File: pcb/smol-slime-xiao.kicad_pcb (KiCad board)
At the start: 4 copper layers, 20 x 23.5 mm, 12 parts, among them J1 Conn_01x02, J2 Conn_01x02, U1 ICM-45686, U3 1532H, U4 XIAO-nRF52840-SMD

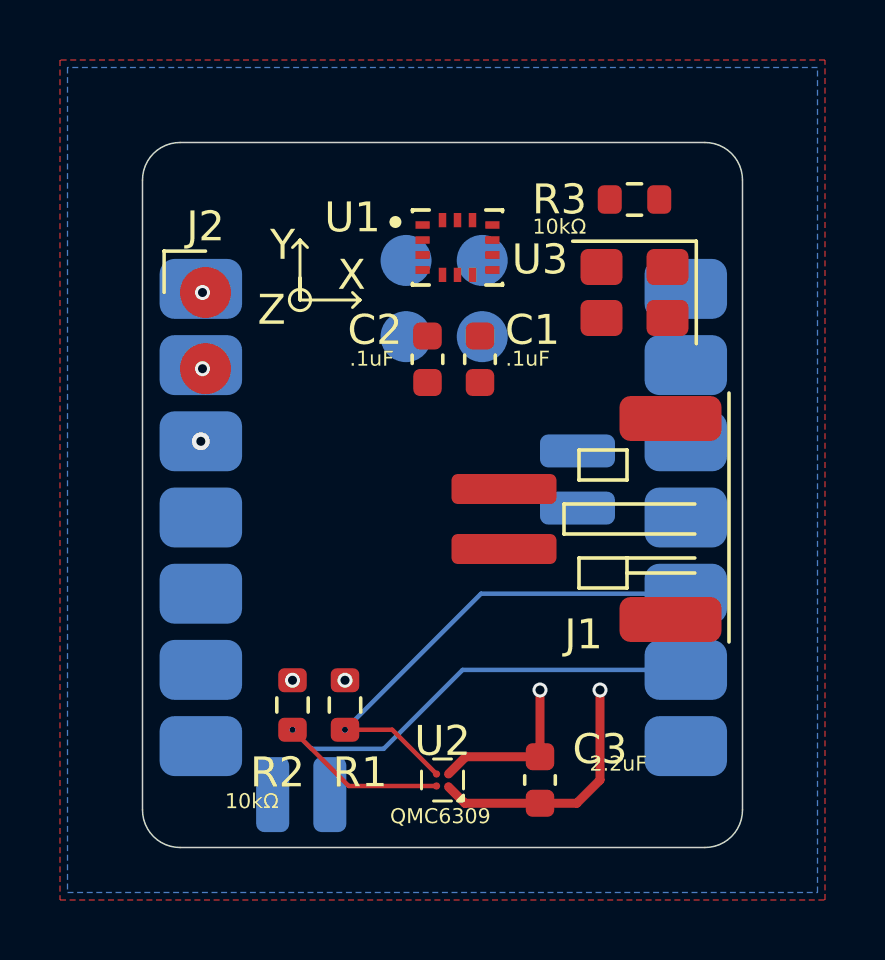
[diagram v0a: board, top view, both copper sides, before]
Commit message: Add JST vias
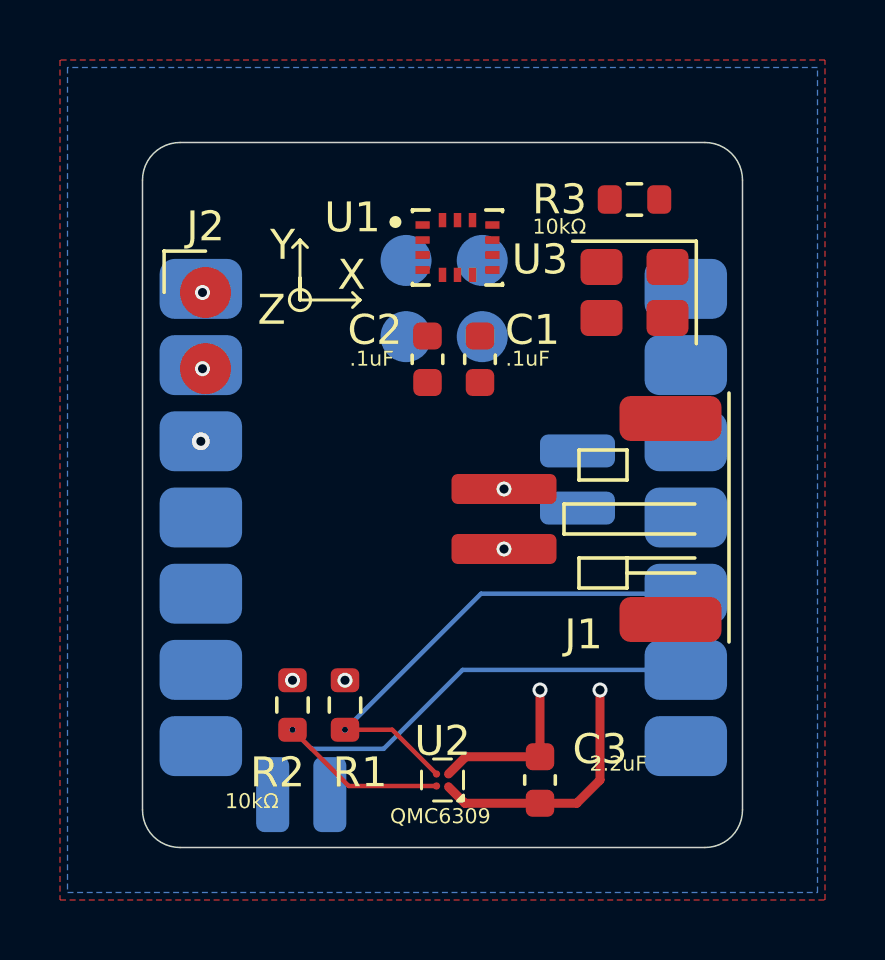
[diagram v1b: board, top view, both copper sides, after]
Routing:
- net GND: vias 2 -> 3
- net /VBAT: vias 0 -> 1
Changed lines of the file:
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@@
+		(net 1)
+	)
+	(via
+		(at 152.05 99.05)
+		(size 0.5)
+		(drill 0.3)
+		(layers "F.Cu" "B.Cu")
 		(net 1)
 	)
@@
 		(net 18)
 	)
+	(via
+		(at 152.05 101.05)
+		(size 0.5)
+		(drill 0.3)
+		(layers "F.Cu" "B.Cu")
+		(net 19)
+	)
 	(zone

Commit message: PCB Current
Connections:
- C2 pad 1: unconnected-(C2-Pad1) -> GND
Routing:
- net GND: vias 3 -> 2
- net +5V: vias 1 -> 0
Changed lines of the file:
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@@
 	(net 18 "+5V")
 	(net 19 "/VBAT")
-	(net 20 "unconnected-(C2-Pad1)")
-	(net 21 "unconnected-(U4-P1.12_D7_RX-Pad8)")
-	(net 22 "unconnected-(U4-NFC1-Pad17)")
-	(net 23 "unconnected-(U4-NFC2-Pad18)")
-	(net 24 "unconnected-(U4-PA31_SWDIO-Pad19)")
-	(net 25 "unconnected-(U4-PA30_SWCLK-Pad20)")
-	(net 26 "unconnected-(U4-P1.11_D6_TX-Pad7)")
-	(net 27 "unconnected-(U4-P0.02_A0_D0-Pad1)")
-	(net 28 "unconnected-(J1-Pin_3-Pad3)")
-	(net 29 "unconnected-(J1-Pin_3-Pad3)_1")
+	(net 20 "unconnected-(U4-P1.12_D7_RX-Pad8)")
+	(net 21 "unconnected-(U4-NFC1-Pad17)")
+	(net 22 "unconnected-(U4-NFC2-Pad18)")
+	(net 23 "unconnected-(U4-PA31_SWDIO-Pad19)")
+	(net 24 "unconnected-(U4-PA30_SWCLK-Pad20)")
+	(net 25 "unconnected-(U4-P1.11_D6_TX-Pad7)")
+	(net 26 "unconnected-(U4-P0.02_A0_D0-Pad1)")
+	(net 27 "unconnected-(J1-Pin_3-Pad3)")
+	(net 28 "unconnected-(J1-Pin_3-Pad3)_1")
 	(footprint "Resistor_SMD:R_0603_1608Metric"
 		(layer "F.Cu")
@@
 			(layers "F.Cu" "F.Mask" "F.Paste")
 			(roundrect_rratio 0.25)
-			(net 28 "unconnected-(J1-Pin_3-Pad3)")
+			(net 28 "unconnected-(J1-Pin_3-Pad3)_1")
 			(pinfunction "Pin_3")
 			(pintype "passive+no_connect")
@@
 			(layers "F.Cu" "F.Mask" "F.Paste")
 			(roundrect_rratio 0.25)
-			(net 29 "unconnected-(J1-Pin_3-Pad3)_1")
+			(net 27 "unconnected-(J1-Pin_3-Pad3)")
 			(pinfunction "Pin_3")
 			(pintype "passive+no_connect")
@@
 			(layers "F.Cu" "F.Mask" "F.Paste")
 			(roundrect_rratio 0.25)
-			(net 20 "unconnected-(C2-Pad1)")
+			(net 1 "GND")
 			(pintype "passive")
 		)
@@
 			(layers "B.Cu" "B.Mask" "B.Paste")
 			(roundrect_rratio 0.25)
-			(net 27 "unconnected-(U4-P0.02_A0_D0-Pad1)")
+			(net 26 "unconnected-(U4-P0.02_A0_D0-Pad1)")
 			(pinfunction "P0.02_A0_D0")
 			(pintype "passive+no_connect")
@@
 			(layers "B.Cu" "B.Mask" "B.Paste")
 			(roundrect_rratio 0.25)
-			(net 26 "unconnected-(U4-P1.11_D6_TX-Pad7)")
+			(net 25 "unconnected-(U4-P1.11_D6_TX-Pad7)")
 			(pinfunction "P1.11_D6_TX")
 			(pintype "passive+no_connect")
@@
 			(layers "B.Cu" "B.Mask" "B.Paste")
 			(roundrect_rratio 0.25)
-			(net 21 "unconnected-(U4-P1.12_D7_RX-Pad8)")
+			(net 20 "unconnected-(U4-P1.12_D7_RX-Pad8)")
 			(pinfunction "P1.12_D7_RX")
 			(pintype "passive+no_connect")
@@
 			(layers "B.Cu" "B.Mask" "B.Paste")
 			(roundrect_rratio 0.25)
-			(net 22 "unconnected-(U4-NFC1-Pad17)")
+			(net 21 "unconnected-(U4-NFC1-Pad17)")
 			(pinfunction "NFC1")
 			(pintype "passive+no_connect")
@@
 			(layers "B.Cu" "B.Mask" "B.Paste")
 			(roundrect_rratio 0.25)
-			(net 23 "unconnected-(U4-NFC2-Pad18)")
+			(net 22 "unconnected-(U4-NFC2-Pad18)")
 			(pinfunction "NFC2")
 			(pintype "passive+no_connect")
@@
 			(size 1.7 1.7)
 			(layers "B.Cu" "B.Mask" "B.Paste")
-			(net 24 "unconnected-(U4-PA31_SWDIO-Pad19)")
+			(net 23 "unconnected-(U4-PA31_SWDIO-Pad19)")
 			(pinfunction "PA31_SWDIO")
 			(pintype "passive+no_connect")
@@
 			(size 1.7 1.7)
 			(layers "B.Cu" "B.Mask" "B.Paste")
-			(net 25 "unconnected-(U4-PA30_SWCLK-Pad20)")
+			(net 24 "unconnected-(U4-PA30_SWCLK-Pad20)")
 			(pinfunction "PA30_SWCLK")
 			(pintype "passive+no_connect")
@@
 	)
 	(via
-		(at 142 95.04)
-		(size 0.5)
-		(drill 0.3)
-		(layers "F.Cu" "B.Cu")
-		(net 1)
-	)
-	(via
 		(at 152.05 99.05)
 		(size 0.5)
@@
 	)
 	(via
-		(at 142 92.5)
-		(size 0.5)
-		(drill 0.3)
-		(layers "F.Cu" "B.Cu")
-		(net 18)
-	)
-	(via

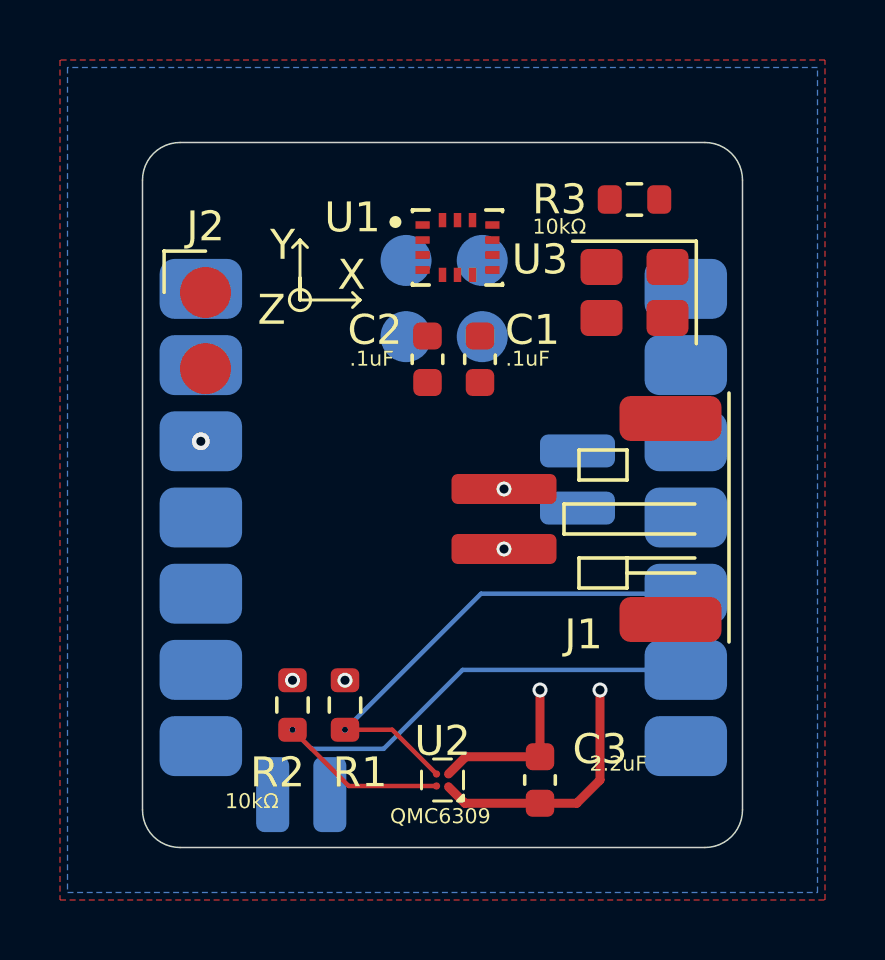
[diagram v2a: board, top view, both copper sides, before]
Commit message: Changed charge connector footprint to 3 pin variant
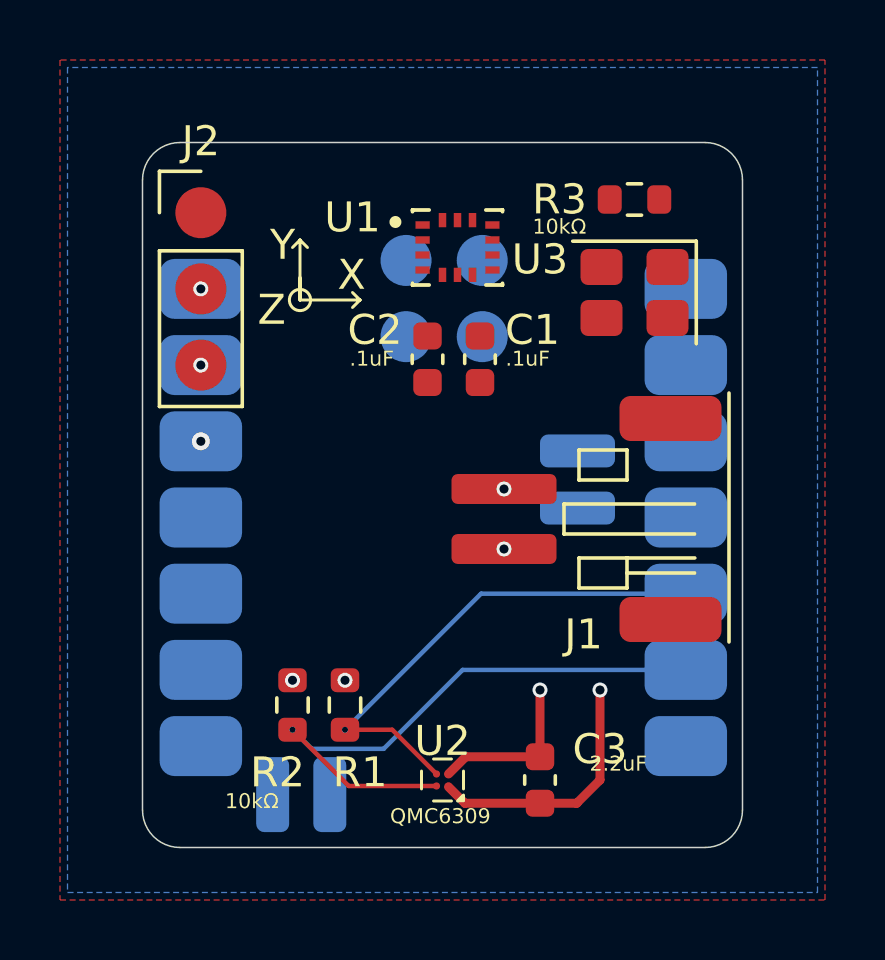
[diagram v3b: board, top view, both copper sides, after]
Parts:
- J1: value Conn_01x02 -> Battery_Terminal
- J2: value Conn_01x02 -> Charger_Connecter; footprint Generic:PinPads_1x02_P2.54mm -> Generic:PinPads_1x03_P2.54mm
- moved J2 2.66 mm to (141.9, 89.8)
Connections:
- J1 pad 2: GND -> /VBAT_GND
- J2 pad 1: +5V -> /VBAT_GND
- J2 pad 2: GND -> +5V
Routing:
- net /VBAT_GND: vias 0 -> 1
- net +5V: vias 0 -> 1
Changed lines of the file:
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@@
 	(net 27 "unconnected-(J1-Pin_3-Pad3)")
 	(net 28 "unconnected-(J1-Pin_3-Pad3)_1")
+	(net 29 "/VBAT_GND")
 	(footprint "Resistor_SMD:R_0603_1608Metric"
 		(layer "F.Cu")
@@
 			)
 		)
-		(property "Value" "Conn_01x02"
+		(property "Value" "Battery_Terminal"
 			(at 1 8.6 90)
 			(layer "F.Fab")
@@
 			(layers "F.Cu" "F.Mask" "F.Paste")
 			(roundrect_rratio 0.2083333333)
-			(net 1 "GND")
+			(net 29 "/VBAT_GND")
 			(pinfunction "Pin_2")
 			(pintype "passive")
@@
 		)
 	)
-	(footprint "Generic:PinPads_1x02_P2.54mm"
+	(footprint "Generic:PinPads_1x03_P2.54mm"
 		(layer "F.Cu")
-		(at 142.1 92.5)
-		(descr "Through hole straight pin header, 1x02, 2.54mm pitch, single row")
-		(tags "Through hole pin header THT 1x02 2.54mm single row")
+		(at 141.945 89.84)
+		(descr "Through hole straight pin header, 1x03, 2.54mm pitch, single row")
+		(tags "Through hole pin header THT 1x03 2.54mm single row")
 		(property "Reference" "J2"
-			(at 0 -2.2 0)
+			(at 0 -2.38 0)
 			(layer "F.SilkS")
 			(effects
@@
 			)
 		)
-		(property "Value" "Conn_01x02"
-			(at 0 4.92 0)
+		(property "Value" "Charger_Connecter"
+			(at 0.7 8.4 0)
 			(layer "F.Fab")
-			(hide yes)
 			(effects
 				(font
@@
 			)
 		)
-		(property "Description" "Generic connector, single row, 01x02, script generated (kicad-library-utils/schlib/autogen/connector/)"
+		(property "Description" "Generic connector, single row, 01x03, script generated (kicad-library-utils/schlib/autogen/connector/)"
 			(at 0 0 0)
 			(layer "F.Fab")
@@
 		)
 		(fp_line
-			(start -1.5 -1.5)
-			(end -1.5 4)
+			(start -1.38 1.27)
+			(end -1.38 6.46)
+			(stroke
+				(width 0.12)
+				(type solid)
+			)
+			(layer "F.SilkS")
+		)
+		(fp_line
+			(start -1.38 1.27)
+			(end 1.38 1.27)
+			(stroke
+				(width 0.12)
+				(type solid)
+			)
+			(layer "F.SilkS")
+		)
+		(fp_line
+			(start -1.38 6.46)
+			(end 1.38 6.46)
+			(stroke
+				(width 0.12)
+				(type solid)
+			)
+			(layer "F.SilkS")
+		)
+		(fp_line
+			(start 1.38 1.27)
+			(end 1.38 6.46)
+			(stroke
+				(width 0.12)
+				(type solid)
+			)
+			(layer "F.SilkS")
+		)
+		(fp_line
+			(start -1.77 -1.77)
+			(end -1.77 6.85)
 			(stroke
 				(width 0.05)
@@
 		)
 		(fp_line
-			(start -1.5 4)
-			(end 1.5 4)
+			(start -1.77 6.85)
+			(end 1.77 6.85)
 			(stroke
 				(width 0.05)
@@
 		)
 		(fp_line
-			(start 1.5 -1.5)
-			(end -1.5 -1.5)
+			(start 1.77 -1.77)
+			(end -1.77 -1.77)
 			(stroke
 				(width 0.05)
@@
 		)
 		(fp_line
-			(start 1.5 4)
-			(end 1.5 -1.5)
+			(start 1.77 6.85)
+			(end 1.77 -1.77)
 			(stroke
 				(width 0.05)
@@
 		)
 		(fp_line
-			(start -1.27 3.81)
+			(start -1.27 6.35)
 			(end -1.27 -0.635)
 			(stroke
@@
 		(fp_line
 			(start 1.27 -1.27)
-			(end 1.27 3.81)
+			(end 1.27 6.35)
 			(stroke
 				(width 0.1)
@@
 		)
 		(fp_line
-			(start 1.27 3.81)
-			(end -1.27 3.81)
+			(start 1.27 6.35)
+			(end -1.27 6.35)
 			(stroke
 				(width 0.1)
@@
 		)
 		(fp_text user "${REFERENCE}"
-			(at 0 -2.25 180)
+			(at 3 2.2 90)
 			(layer "F.Fab")
 			(effects
@@
 			(size 1.7 1.7)
 			(layers "F.Cu" "F.Mask" "F.Paste")
-			(net 18 "+5V")
+			(net 29 "/VBAT_GND")
 			(pinfunction "Pin_1")
 			(pintype "passive")
@@
 			(size 1.7 1.7)
 			(layers "F.Cu" "F.Mask" "F.Paste")
-			(net 1 "GND")
+			(net 18 "+5V")
 			(pinfunction "Pin_2")
 			(pintype "passive")
 		)
+		(pad "3" smd circle
+			(at 0 5.08)
+			(size 1.7 1.7)
+			(layers "F.Cu" "F.Mask" "F.Paste")
+			(net 1 "GND")
+			(pinfunction "Pin_3")
+			(pintype "passive")
+		)
 		(embedded_fonts no)
+		(model "${KICAD9_3DMODEL_DIR}/Connector_PinHeader_2.54mm.3dshapes/PinHeader_1x03_P2.54mm_Vertical.step"
+			(offset
+				(xyz 0 0 0)
+			)
+			(scale
+				(xyz 1 1 1)
+			)
+			(rotate
+				(xyz 0 0 0)
+			)
+		)
 	)
 	(footprint "Capacitor_SMD:C_0603_1608Metric"
@@
 	)
 	(via
-		(at 152.05 99.05)
+		(at 141.945 94.92)
 		(size 0.5)
 		(drill 0.3)
@@
 	)
 	(via
+		(at 141.945 92.38)
+		(size 0.5)
+		(drill 0.3)
+		(layers "F.Cu" "B.Cu")
+		(net 18)
+	)
+	(via
 		(at 152.05 101.05)
 		(size 0.5)
@@
 		(net 19)
 	)
+	(via
+		(at 152.05 99.05)
+		(size 0.5)
+		(drill 0.3)
+		(layers "F.Cu" "B.Cu")
+		(net 29)
+	)
 	(zone

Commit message: Add power switch
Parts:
- added SW1: Power_Switch, SW_SSSS811101:SW_SSSS811101, F.Cu at (150.0, 89.8)
- moved R3 10.9 mm to (146.2, 93.5)
- moved U3 10.8 mm to (146.2, 96.2)
- moved U1 10.0 mm to (145.8, 99.8)
- moved C1 9.42 mm to (146.8, 103.0)
- moved C2 9.42 mm to (145.0, 103.0)
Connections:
- J1 pad 2: /VBAT_GND -> Net-(J1-Pin_2)
- J2 pad 1: /VBAT_GND -> Net-(J2-Pin_1)
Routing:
- net Net-(J1-Pin_2): vias 0 -> 1
- net /VBAT_GND: vias 1 -> 0

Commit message: Reorganise PCB
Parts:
- moved R3 10.9 mm to (156.8, 90.5), turned to -90 degrees
- moved C1 8.81 mm to (147.8, 94.2), turned to -90 degrees
- moved C2 8.75 mm to (145.2, 94.2), turned to -90 degrees
- moved R1 8.00 mm to (154.8, 106.2)
- moved R2 8.00 mm to (153.0, 106.2)
- moved U3 7.65 mm to (153.8, 94.8)
- moved C3 6.28 mm to (147.0, 109.0), turned to 0 degrees
- moved U1 1.85 mm to (146.0, 98.0), turned to 180 degrees
- moved SW1 0.25 mm to (150.0, 89.5)
- turned U2 to 180 degrees
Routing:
- net /SPI_CS_IMU: track 0.00 -> 17.5 mm, vias 0 -> 1
- net /IMU_INT: track 0.00 -> 15.5 mm, vias 0 -> 1
- net /IMU_CLKIN: track 0.00 -> 10.8 mm, vias 0 -> 2
- net /SPI_SCK: track 0.00 -> 9.79 mm, vias 0 -> 1
- net /I2C_SCL: track 20.0 -> 10.4 mm
- net /CLK_CTL: track 0.00 -> 9.21 mm, vias 0 -> 1
- net /SPI_MISO: track 0.00 -> 9.19 mm, vias 0 -> 1
- net Net-(J1-Pin_2): track 0.00 -> 8.71 mm
- net Net-(J2-Pin_1): track 0.00 -> 7.51 mm
- net /SPI_MOSI: track 0.00 -> 6.97 mm, vias 0 -> 1
- net VDD: track 5.51 -> 10.5 mm, vias 4 -> 9
- net /I2C_SDA: track 16.9 -> 13.5 mm
- net /VBAT: track 0.00 -> 3.01 mm
- net GND: track 8.60 -> 10.7 mm, vias 2 -> 5

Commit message: Tied ground vias
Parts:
- added J3: Conn_01x01, Generic:Heat_Pad_1.0x1.0mm, F.Cu at (155.0, 99.8)
- added J4: Conn_01x01, Generic:Heat_Pad_1.0x1.0mm, F.Cu at (155.0, 98.0)
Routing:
- net GND: vias 5 -> 44
- net /VBAT: vias 1 -> 2

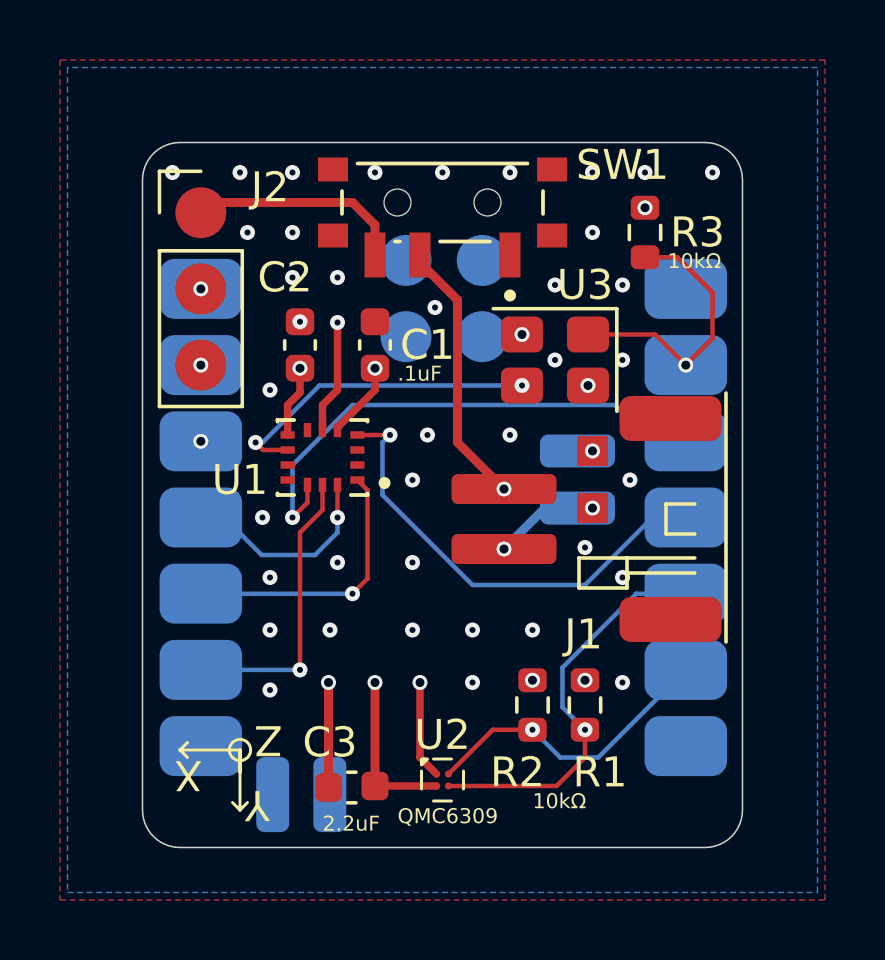
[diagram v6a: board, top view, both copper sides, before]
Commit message: Balance VDD plane GND via cutoffs
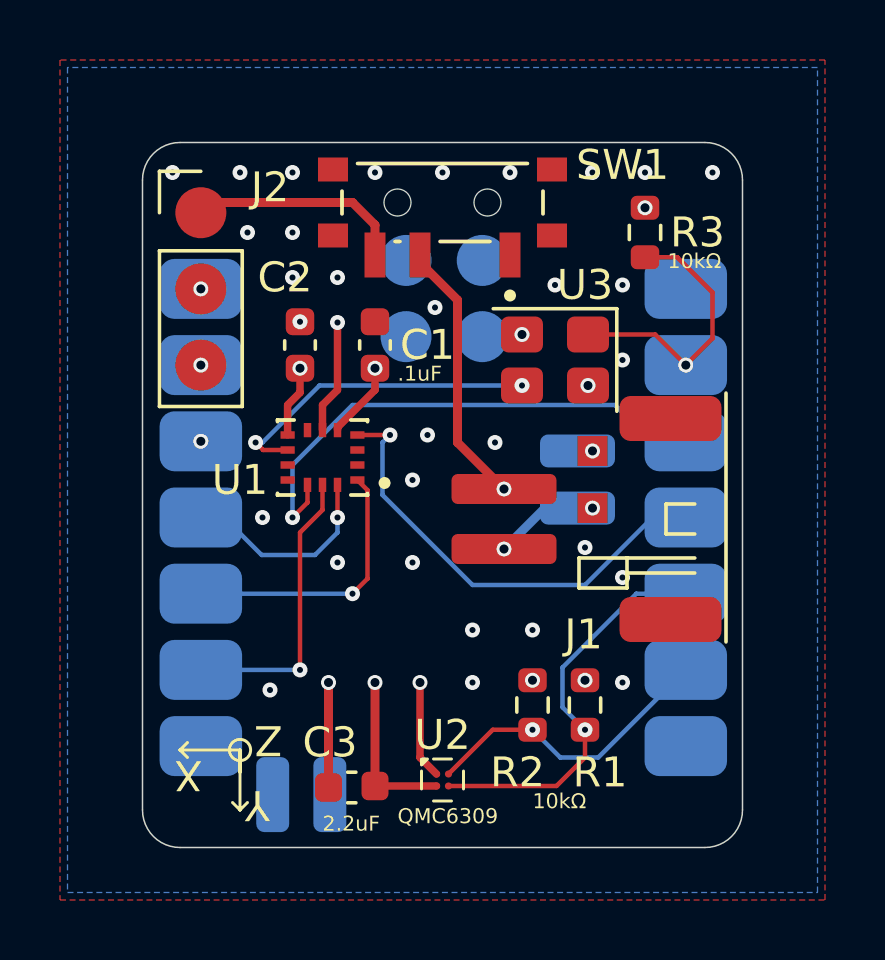
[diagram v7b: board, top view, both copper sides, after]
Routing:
- net GND: vias 44 -> 36
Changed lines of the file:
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@@
-	)
-	(via
-		(at 144.25 103.75)
-		(size 0.5)
-		(drill 0.2)
-		(layers "F.Cu" "B.Cu")
-		(free yes)
-		(net 1)
 	)
 	(via
@@
 	)
 	(via
-		(at 144.25 102)
-		(size 0.5)
-		(drill 0.2)
-		(layers "F.Cu" "B.Cu")
-		(free yes)
-		(net 1)
-	)
-	(via
 		(at 146.5 92)
 		(size 0.5)
@@
 	)
 	(via
-		(at 155 90.5)
-		(size 0.5)
-		(drill 0.2)
-		(layers "F.Cu" "B.Cu")
-		(free yes)
-		(net 1)
-	)
-	(via
 		(at 151 105.5)
 		(size 0.5)
@@
 	)
 	(via
-		(at 149 103.75)
-		(size 0.5)
-		(drill 0.2)
-		(layers "F.Cu" "B.Cu")
-		(free yes)
-		(net 1)
-	)
-	(via
 		(at 151 103.75)
 		(size 0.5)
@@
 	)
 	(via
-		(at 156.25 98.75)
-		(size 0.5)
-		(drill 0.2)
-		(layers "F.Cu" "B.Cu")
-		(free yes)
-		(net 1)
-	)
-	(via
-		(at 144.25 95.75)
-		(size 0.5)
-		(drill 0.2)
-		(layers "F.Cu" "B.Cu")
-		(free yes)
-		(net 1)
-	)
-	(via
 		(at 152.25 88.5)
 		(size 0.5)
@@
 	)
 	(via
-		(at 153.75 94.75)
-		(size 0.5)
-		(drill 0.2)
-		(layers "F.Cu" "B.Cu")
-		(free yes)
-		(net 1)
-	)
-	(via
-		(at 146.25 103.75)
-		(size 0.5)
-		(drill 0.2)
-		(layers "F.Cu" "B.Cu")
-		(free yes)
-		(net 1)
-	)
-	(via
 		(at 156 94.75)
 		(size 0.5)
@@
 	)
 	(via
-		(at 152.25 97.25)
-		(size 0.5)
-		(drill 0.2)
+		(at 151.75 97.5)
+		(size 0.5)
+		(drill 0.2)
